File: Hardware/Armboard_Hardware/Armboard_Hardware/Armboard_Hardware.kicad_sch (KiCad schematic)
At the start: 237 parts, among them J1 RJ45_LED_Shielded, J2 Conn_02x03_Counter_Clockwise, Q1 SI4156DY, Q10 SI4156DY, Q11 SI4156DY, Q12 SI4156DY, Q13 SI4156DY, Q14 SI4156DY, Q15 SI4156DY, Q16 SI4156DY, Q17 SI4156DY, Q18 SI4156DY, Q19 SI4156DY, Q2 SI4156DY, Q20 SI4156DY, Q21 SI4156DY, Q22 SI4156DY, Q23 SI4156DY, Q24 SI4156DY, Q25 SI4156DY, Q26 SI4156DY, Q27 SI4156DY, Q28 SI4156DY, Q29 BSS138, Q3 SI4156DY, Q30 SI4156DY, Q31 SI4156DY, Q32 SI4156DY, Q33 SI4156DY, Q34 SI4156DY, Q35 SI4156DY, Q36 SI4156DY, Q37 SI4156DY, Q38 BSS138, Q4 SI4156DY, Q5 SI4156DY, Q6 SI4156DY, Q7 SI4156DY, Q8 SI4156DY, Q9 SI4156DY, U1 Teensy4.1_DEV-16771, U10 IRS2005S, U11 IRS2005S, U12 IRS2005S, U13 IRS2005S, U14 OKI, U15 IRS2005S, U16 IRS2005S, U17 IRS2005S, U18 IRS2005S, U19 IRS2005S, U2 IRS2005S, U20 IRS2005S, U21 74LVC2G04, U22 74LVC2G04, U23 74LVC2G04, U24 74LVC2G04, U25 74LVC2G04, U26 74LVC2G04, U27 74LVC2G04, U28 74LVC2G04, U29 74LVC2G04, U3 IRS2005S, U4 IRS2005S, U5 IRS2005S, U6 IRS2005S, U7 IRS2005S, U8 IRS2005S, U9 IRS2005S

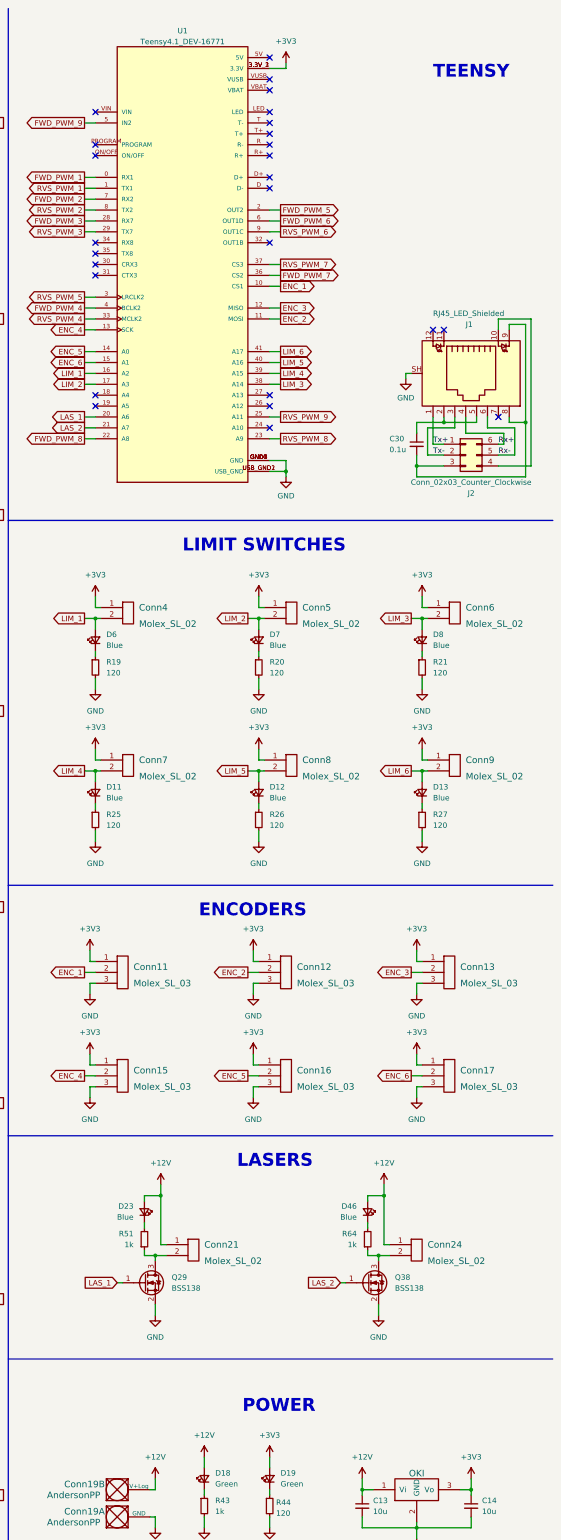
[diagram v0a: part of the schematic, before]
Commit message: Enlarged 12V Plane, reran traces for ground continuity
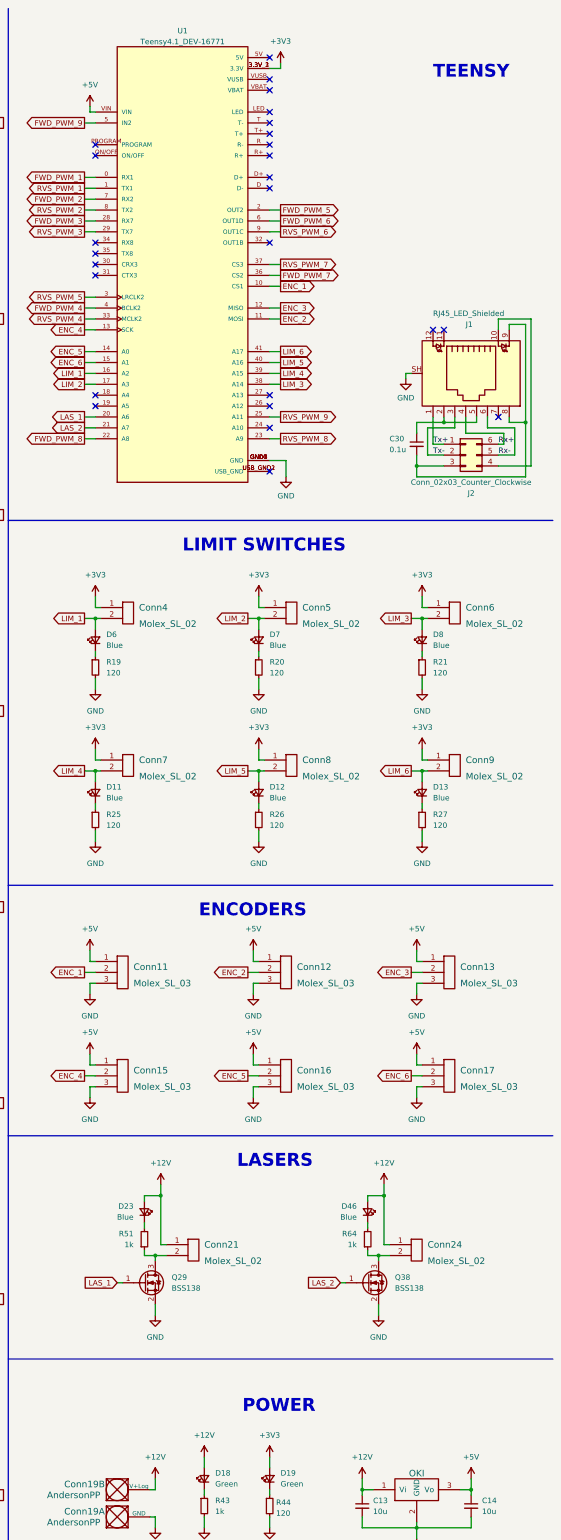
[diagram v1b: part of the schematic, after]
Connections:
- net +3V3: no longer C14.1, Conn11.1, Conn12.1, Conn13.1, Conn15.1, Conn16.1, Conn17.1, U14.3 (Vo)
- net GND: no longer U1.USB_GND1 (USB_GND), U1.USB_GND2 (USB_GND)
- net +5V: now reaches U1.VIN
- net +5V: now also C14.1, Conn11.1, Conn12.1, Conn13.1, Conn15.1, Conn16.1, Conn17.1, U14.3 (Vo)
- new net: U1.USB_GND1 (USB_GND), U1.USB_GND2 (USB_GND)

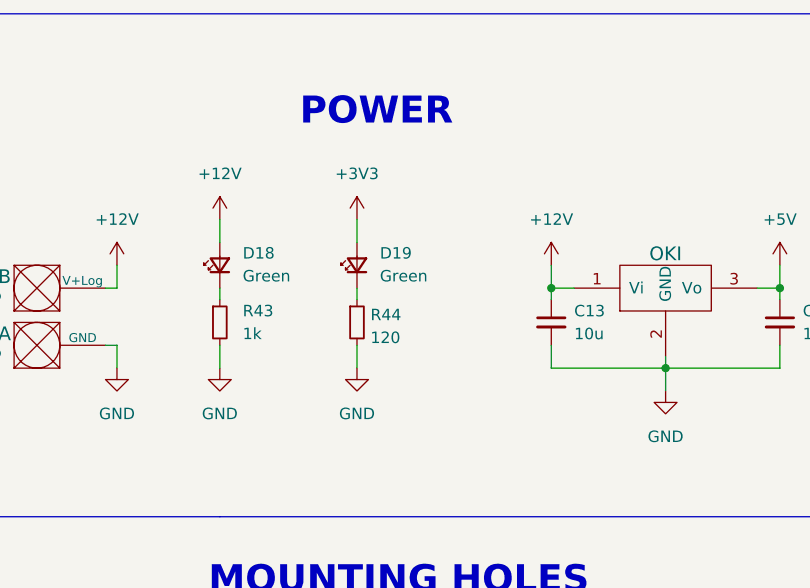
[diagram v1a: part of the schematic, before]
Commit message: Added 5V LED and adjusted FWD and RVS PWM LEDs
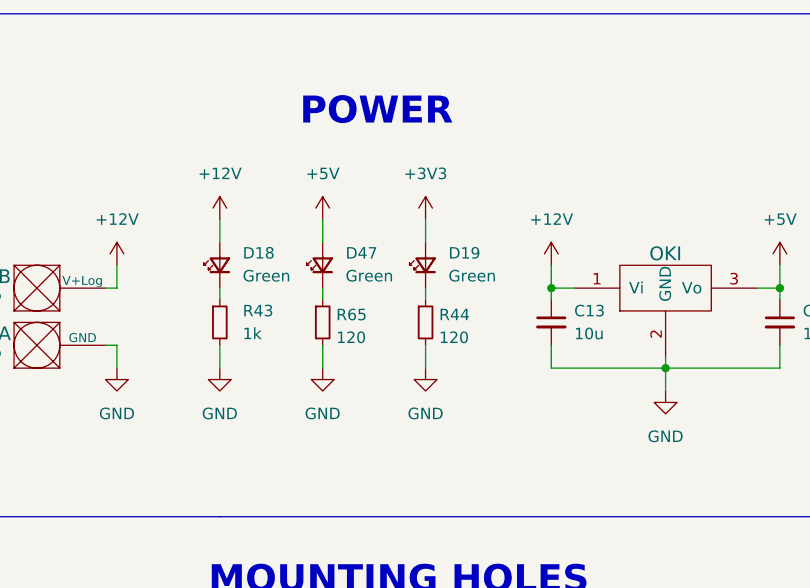
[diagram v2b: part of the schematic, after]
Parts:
- added D47: Green, LED_SMD:LED_0603_1608Metric_Pad1.05x0.95mm_HandSolder, symbol Device:LED_Small
- added R65: 120, Resistor_SMD:R_0603_1608Metric_Pad0.98x0.95mm_HandSolder, symbol Device:R_Small
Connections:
- net +5V: now also D47.2 (A)
- net GND: now also R65.2
- new net: D47.1 (K), R65.1
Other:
- moved on the sheet: D19, R44
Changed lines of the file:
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@@
     (stroke (width 0) (type default) (color 0 0 0 0))
   )
-  (wire (pts (xy 271.78 356.87) (xy 271.78 358.14))
+  (wire (pts (xy 279.4 356.87) (xy 279.4 358.14))
     (stroke (width 0) (type default) (color 0 0 0 0))
   )
@@
     (stroke (width 0) (type default) (color 0 0 0 0))
   )
+  (wire (pts (xy 267.97 349.25) (xy 267.97 351.79))
+    (stroke (width 0) (type default) (color 0 0 0 0))
+  )
   (wire (pts (xy 83.82 424.18) (xy 83.82 426.72))
     (stroke (width 0) (type default) (color 0 0 0 0))
@@
     (stroke (width 0) (type default) (color 0 0 0 0))
   )
-  (wire (pts (xy 271.78 363.22) (xy 271.78 365.76))
+  (wire (pts (xy 279.4 363.22) (xy 279.4 365.76))
     (stroke (width 0) (type default) (color 0 0 0 0))
   )
@@
     (stroke (width 0) (type default) (color 0 0 0 0))
   )
+  (wire (pts (xy 267.97 363.22) (xy 267.97 365.76))
+    (stroke (width 0) (type default) (color 0 0 0 0))
+  )
   (wire (pts (xy 269.24 167.64) (xy 269.24 170.18))
     (stroke (width 0) (type default) (color 0 0 0 0))
@@
     (stroke (width 0) (type default) (color 0 0 0 0))
   )
+  (wire (pts (xy 267.97 356.87) (xy 267.97 358.14))
+    (stroke (width 0) (type default) (color 0 0 0 0))
+  )
   (wire (pts (xy 139.7 91.44) (xy 139.7 92.71))
     (stroke (width 0) (type default) (color 0 0 0 0))
@@
     (stroke (width 0) (type default) (color 0 0 0 0))
   )
-  (wire (pts (xy 271.78 349.25) (xy 271.78 351.79))
+  (wire (pts (xy 279.4 349.25) (xy 279.4 351.79))
     (stroke (width 0) (type default) (color 0 0 0 0))
   )
@@
     (pin "1")
   )
+  (symbol (lib_id "Device:R_Small") (at 267.97 360.68 0) (unit 1)
+    (in_bom yes) (on_board yes) (fields_autoplaced)
+    (property "Reference" "R65" (id 0) (at 269.4686 359.8453 0)
+      (effects (font (size 1.27 1.27)) (justify left))
+    )
+    (property "Value" "120" (id 1) (at 269.4686 362.3822 0)
+      (effects (font (size 1.27 1.27)) (justify left))
+    )
+    (property "Footprint" "Resistor_SMD:R_0603_1608Metric_Pad0.98x0.95mm_HandSolder" (id 2) (at 267.97 360.68 0)
+      (effects (font (size 1.27 1.27)) hide)
+    )
+    (property "Datasheet" "~" (id 3) (at 267.97 360.68 0)
+      (effects (font (size 1.27 1.27)) hide)
+    )
+    (pin "1")
+    (pin "2")
+  )
   (symbol (lib_id "Device:R_Small") (at 27.94 195.58 0) (mirror x) (unit 1)
     (in_bom yes) (on_board yes) (fields_autoplaced)
@@
     (pin "8")
   )
-  (symbol (lib_id "power:+3V3") (at 271.78 349.25 0) (unit 1)
+  (symbol (lib_id "power:+3V3") (at 279.4 349.25 0) (unit 1)
     (in_bom yes) (on_board yes) (fields_autoplaced)
-    (property "Reference" "#PWR0166" (id 0) (at 271.78 353.06 0)
+    (property "Reference" "#PWR0166" (id 0) (at 279.4 353.06 0)
       (effects (font (size 1.27 1.27)) hide)
     )
-    (property "Value" "+3V3" (id 1) (at 271.78 344.17 0))
-    (property "Footprint" "" (id 2) (at 271.78 349.25 0)
+    (property "Value" "+3V3" (id 1) (at 279.4 344.17 0))
+    (property "Footprint" "" (id 2) (at 279.4 349.25 0)
       (effects (font (size 1.27 1.27)) hide)
     )
-    (property "Datasheet" "" (id 3) (at 271.78 349.25 0)
+    (property "Datasheet" "" (id 3) (at 279.4 349.25 0)
       (effects (font (size 1.27 1.27)) hide)
     )
@@
     (pin "2")
   )
+  (symbol (lib_id "Device:LED_Small") (at 267.97 354.33 90) (unit 1)
+    (in_bom yes) (on_board yes)
+    (property "Reference" "D47" (id 0) (at 270.51 352.9964 90)
+      (effects (font (size 1.27 1.27)) (justify right))
+    )
+    (property "Value" "Green" (id 1) (at 270.51 355.5364 90)
+      (effects (font (size 1.27 1.27)) (justify right))
+    )
+    (property "Footprint" "LED_SMD:LED_0603_1608Metric_Pad1.05x0.95mm_HandSolder" (id 2) (at 267.97 354.33 90)
+      (effects (font (size 1.27 1.27)) hide)
+    )
+    (property "Datasheet" "~" (id 3) (at 267.97 354.33 90)
+      (effects (font (size 1.27 1.27)) hide)
+    )
+    (pin "1")
+    (pin "2")
+  )
   (symbol (lib_id "MRDT_Drill_Holes:Via") (at 247.65 397.51 0) (unit 1)
     (in_bom yes) (on_board yes) (fields_autoplaced)
@@
     (pin "8")
   )
-  (symbol (lib_id "Device:R_Small") (at 271.78 360.68 0) (unit 1)
+  (symbol (lib_id "Device:R_Small") (at 279.4 360.68 0) (unit 1)
     (in_bom yes) (on_board yes) (fields_autoplaced)
-    (property "Reference" "R44" (id 0) (at 273.2786 359.8453 0)
+    (property "Reference" "R44" (id 0) (at 280.8986 359.8453 0)
       (effects (font (size 1.27 1.27)) (justify left))
     )
-    (property "Value" "120" (id 1) (at 273.2786 362.3822 0)
+    (property "Value" "120" (id 1) (at 280.8986 362.3822 0)
       (effects (font (size 1.27 1.27)) (justify left))
     )
-    (property "Footprint" "Resistor_SMD:R_0603_1608Metric_Pad0.98x0.95mm_HandSolder" (id 2) (at 271.78 360.68 0)
+    (property "Footprint" "Resistor_SMD:R_0603_1608Metric_Pad0.98x0.95mm_HandSolder" (id 2) (at 279.4 360.68 0)
       (effects (font (size 1.27 1.27)) hide)
     )
-    (property "Datasheet" "~" (id 3) (at 271.78 360.68 0)
+    (property "Datasheet" "~" (id 3) (at 279.4 360.68 0)
       (effects (font (size 1.27 1.27)) hide)
     )
@@
     (pin "2")
   )
+  (symbol (lib_id "power:GND") (at 267.97 365.76 0) (unit 1)
+    (in_bom yes) (on_board yes) (fields_autoplaced)
+    (property "Reference" "#PWR06" (id 0) (at 267.97 372.11 0)
+      (effects (font (size 1.27 1.27)) hide)
+    )
+    (property "Value" "GND" (id 1) (at 267.97 370.84 0))
+    (property "Footprint" "" (id 2) (at 267.97 365.76 0)
+      (effects (font (size 1.27 1.27)) hide)
+    )
+    (property "Datasheet" "" (id 3) (at 267.97 365.76 0)
+      (effects (font (size 1.27 1.27)) hide)
+    )
+    (pin "1")
+  )
   (symbol (lib_id "Transistor_FET:FDS2734") (at 81.28 314.96 0) (unit 1)
     (in_bom yes) (on_board yes)
@@
     (pin "SH")
   )
-  (symbol (lib_id "power:GND") (at 271.78 365.76 0) (unit 1)
+  (symbol (lib_id "power:GND") (at 279.4 365.76 0) (unit 1)
     (in_bom yes) (on_board yes) (fields_autoplaced)
-    (property "Reference" "#PWR0164" (id 0) (at 271.78 372.11 0)
+    (property "Reference" "#PWR0164" (id 0) (at 279.4 372.11 0)
       (effects (font (size 1.27 1.27)) hide)
     )
-    (property "Value" "GND" (id 1) (at 271.78 370.84 0))
-    (property "Footprint" "" (id 2) (at 271.78 365.76 0)
+    (property "Value" "GND" (id 1) (at 279.4 370.84 0))
+    (property "Footprint" "" (id 2) (at 279.4 365.76 0)
       (effects (font (size 1.27 1.27)) hide)
     )
-    (property "Datasheet" "" (id 3) (at 271.78 365.76 0)
+    (property "Datasheet" "" (id 3) (at 279.4 365.76 0)
       (effects (font (size 1.27 1.27)) hide)
     )
@@
     (pin "2")
   )
-  (symbol (lib_id "Device:LED_Small") (at 271.78 354.33 90) (unit 1)
+  (symbol (lib_id "Device:LED_Small") (at 279.4 354.33 90) (unit 1)
     (in_bom yes) (on_board yes)
-    (property "Reference" "D19" (id 0) (at 274.32 352.9964 90)
+    (property "Reference" "D19" (id 0) (at 281.94 352.9964 90)
       (effects (font (size 1.27 1.27)) (justify right))
     )
-    (property "Value" "Green" (id 1) (at 274.32 355.5364 90)
+    (property "Value" "Green" (id 1) (at 281.94 355.5364 90)
       (effects (font (size 1.27 1.27)) (justify right))
     )
-    (property "Footprint" "LED_SMD:LED_0603_1608Metric_Pad1.05x0.95mm_HandSolder" (id 2) (at 271.78 354.33 90)
+    (property "Footprint" "LED_SMD:LED_0603_1608Metric_Pad1.05x0.95mm_HandSolder" (id 2) (at 279.4 354.33 90)
       (effects (font (size 1.27 1.27)) hide)
     )
-    (property "Datasheet" "~" (id 3) (at 271.78 354.33 90)
+    (property "Datasheet" "~" (id 3) (at 279.4 354.33 90)
       (effects (font (size 1.27 1.27)) hide)
     )
@@
     (pin "1")
   )
+  (symbol (lib_id "power:+5V") (at 267.97 349.25 0) (unit 1)
+    (in_bom yes) (on_board yes) (fields_autoplaced)
+    (property "Reference" "#PWR03" (id 0) (at 267.97 353.06 0)
+      (effects (font (size 1.27 1.27)) hide)
+    )
+    (property "Value" "+5V" (id 1) (at 267.97 344.17 0))
+    (property "Footprint" "" (id 2) (at 267.97 349.25 0)
+      (effects (font (size 1.27 1.27)) hide)
+    )
+    (property "Datasheet" "" (id 3) (at 267.97 349.25 0)
+      (effects (font (size 1.27 1.27)) hide)
+    )
+    (pin "1")
+  )
   (symbol (lib_id "power:+3V3") (at 182.88 318.77 0) (unit 1)
     (in_bom yes) (on_board yes) (fields_autoplaced)
@@
       (reference "#PWR02") (unit 1) (value "+12V") (footprint "")
     )
+    (path "/fa514135-0e2b-47a0-ac01-376480a5c227"
+      (reference "#PWR03") (unit 1) (value "+5V") (footprint "")
+    )
     (path "/b4b2c192-db80-4718-b644-a8bdf1c94f5f"
       (reference "#PWR04") (unit 1) (value "+12V") (footprint "")
@@
       (reference "#PWR05") (unit 1) (value "+12V") (footprint "")
     )
+    (path "/d2bb1e30-bb1b-424d-a5e9-9f35fcff3d55"
+      (reference "#PWR06") (unit 1) (value "GND") (footprint "")
+    )
     (path "/d658e52a-25ea-458b-b6a5-a4c476a9219a"
       (reference "#PWR09") (unit 1) (value "GND") (footprint "")
@@
       (reference "D46") (unit 1) (value "Blue") (footprint "LED_SMD:LED_0603_1608Metric_Pad1.05x0.95mm_HandSolder")
     )
+    (path "/80f015e6-a2c1-4340-b8e0-eea008eca89f"
+      (reference "D47") (unit 1) (value "Green") (footprint "LED_SMD:LED_0603_1608Metric_Pad1.05x0.95mm_HandSolder")
+    )
     (path "/d71700fe-7146-4948-ad1a-0a192eb569d2"
       (reference "J1") (unit 1) (value "RJ45_LED_Shielded") (footprint "MRDT_Connectors:RJ45_Teensy")
@@
       (reference "R64") (unit 1) (value "1k") (footprint "Resistor_SMD:R_0603_1608Metric_Pad0.98x0.95mm_HandSolder")
     )
+    (path "/01bfa802-1f90-4595-b1ee-e1ef20ac18a1"
+      (reference "R65") (unit 1) (value "120") (footprint "Resistor_SMD:R_0603_1608Metric_Pad0.98x0.95mm_HandSolder")
+    )
     (path "/1589b590-5572-4d4d-93a2-cbd99023117f"
